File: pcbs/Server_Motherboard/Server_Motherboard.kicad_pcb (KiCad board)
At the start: 2 copper layers, 53 x 70.4 mm, 96 parts, among them IC1 BTM9011EPXUMA1, IC10 BTM9011EPXUMA1, IC11 BTM9011EPXUMA1, IC12 BTM9011EPXUMA1, IC13 BTM9011EPXUMA1, IC14 BTM9011EPXUMA1, IC15 BTM9011EPXUMA1, IC16 BTM9011EPXUMA1, IC17 BTM9011EPXUMA1, IC18 BTM9011EPXUMA1, IC19 BTM9011EPXUMA1, IC2 BTM9011EPXUMA1, IC20 BTM9011EPXUMA1, IC3 BTM9011EPXUMA1, IC4 BTM9011EPXUMA1, IC5 BTM9011EPXUMA1, IC6 BTM9011EPXUMA1, IC7 BTM9011EPXUMA1, IC8 BTM9011EPXUMA1, IC9 BTM9011EPXUMA1, J1 GSB1C41110SSHR, U1 ESP32-C3-MINI-1-H4X

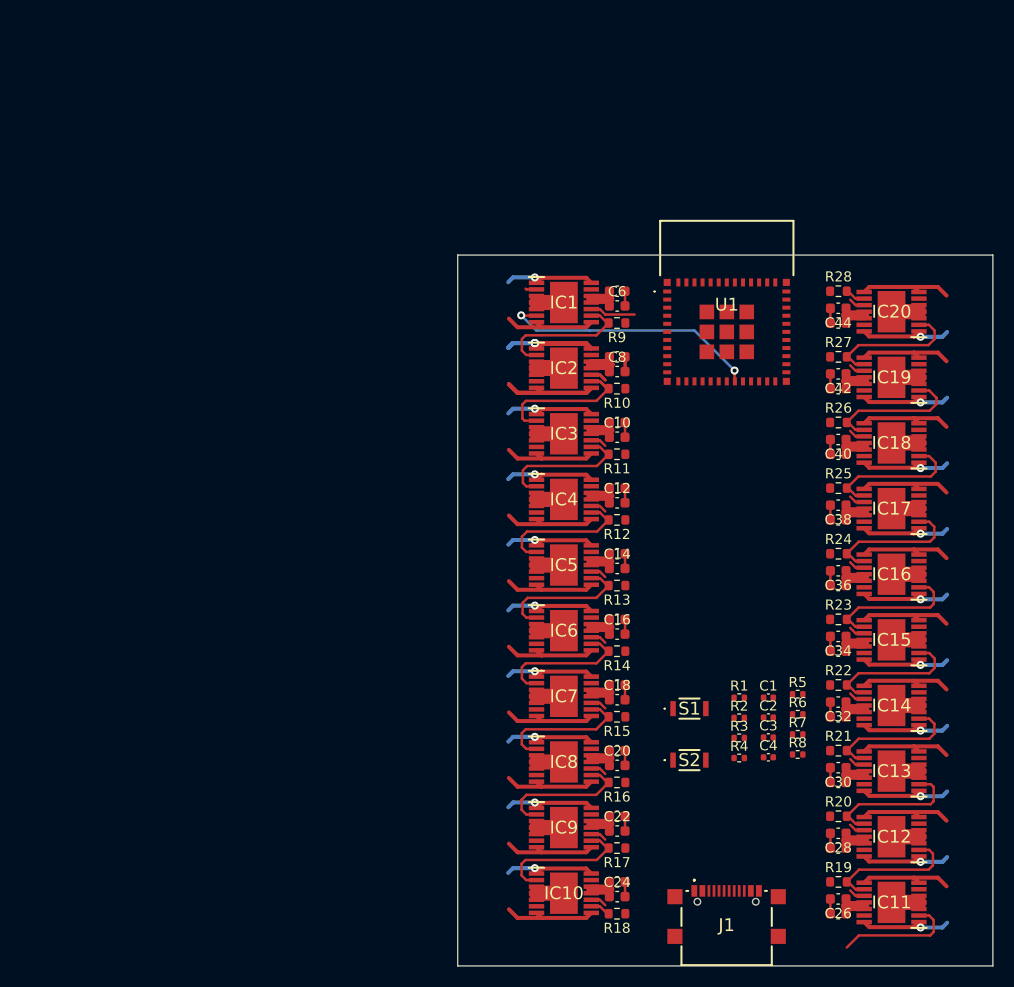
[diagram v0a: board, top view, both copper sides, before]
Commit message: mostly finished server pcb, added pogo charge pins to bots, started charge case pcb
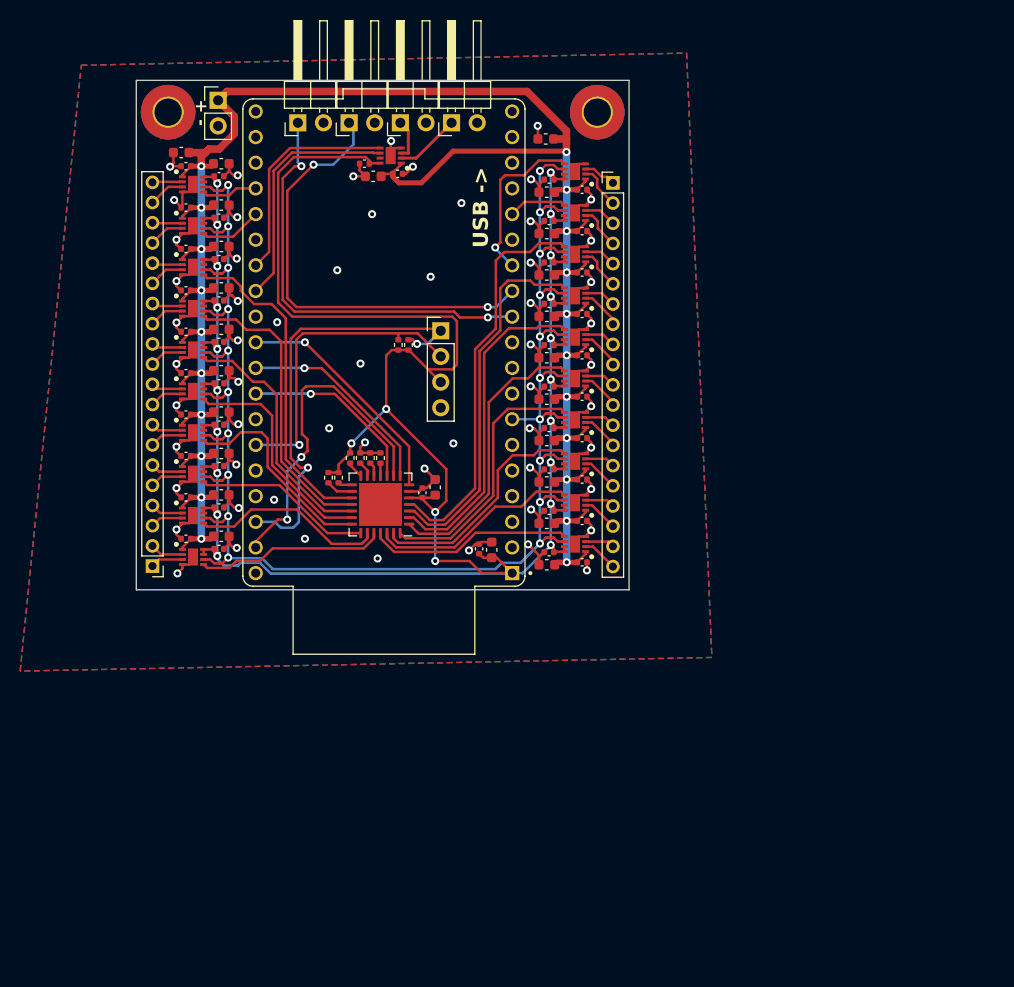
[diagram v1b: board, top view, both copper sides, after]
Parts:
- removed IC10, IC11, IC12, IC13, IC14, IC15, IC16, IC17, IC18, IC19, IC2, IC20, IC3, IC4, IC5, IC6, IC7, IC8, IC9: BTM9011EPXUMA1, SamacSys_Parts:SOP65P600X115-15N
- removed R10, R11, R12, R13, R14, R15, R16, R17, R18, R19, R20, R21, R22, R23, R24, R25, R26, R27, R28, R9: 1k, Resistor_SMD:R_0603_1608Metric
- removed S1, S2: EVP-AWBD4A, SamacSys_Parts:EVPAWBD4A
- added C45: 0.1uF, Capacitor_SMD:C_0402_1005Metric, F.Cu at (57.1, 50.9)
- added C46: 0.1uF, Capacitor_SMD:C_0402_1005Metric, F.Cu at (57.1, 55.0)
- added C47: 0.1uF, Capacitor_SMD:C_0402_1005Metric, F.Cu at (57.1, 59.1)
- added C48: 0.1uF, Capacitor_SMD:C_0402_1005Metric, F.Cu at (57.1, 63.2)
- added C49: 0.1uF, Capacitor_SMD:C_0402_1005Metric, F.Cu at (57.1, 67.3)
- added C50: 0.1uF, Capacitor_SMD:C_0402_1005Metric, F.Cu at (57.1, 71.4)
- added C51: 0.1uF, Capacitor_SMD:C_0402_1005Metric, F.Cu at (57.1, 75.5)
- added C52: 0.1uF, Capacitor_SMD:C_0402_1005Metric, F.Cu at (57.1, 79.6)
- added C53: 0.1uF, Capacitor_SMD:C_0402_1005Metric, F.Cu at (89.8, 79.9)
- added C54: 0.1uF, Capacitor_SMD:C_0402_1005Metric, F.Cu at (89.8, 75.8)
- added C55: 0.1uF, Capacitor_SMD:C_0402_1005Metric, F.Cu at (89.8, 71.7)
- added C56: 0.1uF, Capacitor_SMD:C_0402_1005Metric, F.Cu at (89.8, 67.6)
- added C57: 0.1uF, Capacitor_SMD:C_0402_1005Metric, F.Cu at (89.8, 63.5)
- added C58: 0.1uF, Capacitor_SMD:C_0402_1005Metric, F.Cu at (89.8, 59.4)
- added C59: 0.1uF, Capacitor_SMD:C_0402_1005Metric, F.Cu at (89.8, 55.3)
- added C60: 0.1uF, Capacitor_SMD:C_0402_1005Metric, F.Cu at (89.8, 51.2)
- added C61: 0.1uF, Capacitor_SMD:C_0402_1005Metric, F.Cu at (89.8, 47.1)
- added C62: 0.1uF, Capacitor_SMD:C_0402_1005Metric, F.Cu at (89.8, 43.0)
- added C63: 0.1uF, Capacitor_SMD:C_0402_1005Metric, F.Cu at (77.2, 74.0)
- added C64: 10uF, Capacitor_SMD:C_0603_1608Metric, F.Cu at (78.5, 73.5)
- added C65: 10uF, Capacitor_SMD:C_0603_1608Metric, F.Cu at (84.1, 79.7)
- added C66: 10uF, Capacitor_SMD:C_0603_1608Metric, F.Cu at (89.5, 39.0)
- added C67: 0.1uF, Capacitor_SMD:C_0402_1005Metric, F.Cu at (71.5, 41.4)
- added C68: 10uF, Capacitor_SMD:C_0603_1608Metric, F.Cu at (72.4, 42.6)
- added C69: 0.1uF, Capacitor_SMD:C_0402_1005Metric, F.Cu at (74.8, 42.4)
- added H1: MountingHole_Pad, MountingHole:MountingHole_2.7mm_M2.5_Pad_TopBottom, F.Cu at (52.0, 36.3)
- added H2: MountingHole_Pad, MountingHole:MountingHole_2.7mm_M2.5_Pad_TopBottom, F.Cu at (94.5, 36.3)
- added IC21: DRV8210DSGR, minibot:SON50P200X200X80-9N, F.Cu at (54.5, 43.5)
- added IC22: DRV8210DSGR, minibot:SON50P200X200X80-9N, F.Cu at (54.5, 47.5)
- added IC23: DRV8210DSGR, minibot:SON50P200X200X80-9N, F.Cu at (54.5, 51.6)
- added IC24: DRV8210DSGR, minibot:SON50P200X200X80-9N, F.Cu at (54.5, 55.8)
- added IC25: DRV8210DSGR, minibot:SON50P200X200X80-9N, F.Cu at (54.5, 59.9)
- added IC26: DRV8210DSGR, minibot:SON50P200X200X80-9N, F.Cu at (54.5, 64.0)
- added IC27: DRV8210DSGR, minibot:SON50P200X200X80-9N, F.Cu at (54.5, 68.0)
- added IC28: DRV8210DSGR, minibot:SON50P200X200X80-9N, F.Cu at (54.5, 72.2)
- added IC29: DRV8210DSGR, minibot:SON50P200X200X80-9N, F.Cu at (54.5, 76.2)
- added IC30: DRV8210DSGR, minibot:SON50P200X200X80-9N, F.Cu at (54.5, 80.3)
- added IC31: DRV8210DSGR, minibot:SON50P200X200X80-9N, F.Cu at (92.4, 79.1)
- added IC32: DRV8210DSGR, minibot:SON50P200X200X80-9N, F.Cu at (92.4, 75.0)
- added IC33: DRV8210DSGR, minibot:SON50P200X200X80-9N, F.Cu at (92.4, 70.9)
- added IC34: DRV8210DSGR, minibot:SON50P200X200X80-9N, F.Cu at (92.4, 66.8)
- added IC35: DRV8210DSGR, minibot:SON50P200X200X80-9N, F.Cu at (92.4, 62.7)
- added IC36: DRV8210DSGR, minibot:SON50P200X200X80-9N, F.Cu at (92.4, 58.6)
- added IC37: DRV8210DSGR, minibot:SON50P200X200X80-9N, F.Cu at (92.4, 54.5)
- added IC38: DRV8210DSGR, minibot:SON50P200X200X80-9N, F.Cu at (92.4, 50.4)
- added IC39: DRV8210DSGR, minibot:SON50P200X200X80-9N, F.Cu at (92.4, 46.3)
- added IC40: DRV8210DSGR, minibot:SON50P200X200X80-9N, F.Cu at (92.4, 42.2)
- added J2: Conn_01x20, Connector_PinHeader_2.00mm:PinHeader_1x20_P2.00mm_Vertical, F.Cu at (96.1, 43.3)
- added J3: Conn_01x02, Connector_PinHeader_2.54mm:PinHeader_1x02_P2.54mm_Vertical, F.Cu at (57.0, 35.1)
- added J4: Conn_01x04, Connector_PinHeader_2.54mm:PinHeader_1x04_P2.54mm_Vertical, F.Cu at (79.0, 58.0)
- added J5: Conn_01x02, Connector_PinHeader_2.54mm:PinHeader_1x02_P2.54mm_Horizontal, F.Cu at (75.0, 37.4)
- added J6: Conn_01x02, Connector_PinHeader_2.54mm:PinHeader_1x02_P2.54mm_Horizontal, F.Cu at (80.1, 37.4)
- added J7: Conn_01x02, Connector_PinHeader_2.54mm:PinHeader_1x02_P2.54mm_Horizontal, F.Cu at (64.9, 37.4)
- added J8: Conn_01x02, Connector_PinHeader_2.54mm:PinHeader_1x02_P2.54mm_Horizontal, F.Cu at (70.0, 37.4)
- added U2: MCP23S17_ML, Package_DFN_QFN:QFN-28-1EP_6x6mm_P0.65mm_EP4.25x4.25mm, F.Cu at (73.1, 75.2)
- C1: value 4.7uF -> 10uF; footprint Capacitor_SMD:C_0402_1005Metric -> Capacitor_SMD:C_0603_1608Metric
- C10, C12, C14, C16, C18, C20, C22, C24, C26, C28, C30, C32, C34, C36, C38, C40, C42, C44, C6, C8: footprint Capacitor_SMD:C_0603_1608Metric -> Capacitor_SMD:C_0402_1005Metric
- C2: value 1uF -> 0.1uF
- C3: value 0.1uF -> 10uF; footprint Capacitor_SMD:C_0402_1005Metric -> Capacitor_SMD:C_0603_1608Metric
- C43: value 10uF -> 0.1uF; footprint Capacitor_SMD:C_0603_1608Metric -> Capacitor_SMD:C_0402_1005Metric
- IC1: value BTM9011EPXUMA1 -> DRV8210DSGR; footprint SamacSys_Parts:SOP65P600X115-15N -> minibot:SON50P200X200X80-9N
- J1: value GSB1C41110SSHR -> Conn_01x20; footprint SamacSys_Parts:GSB1C41110SSHR -> Connector_PinHeader_2.00mm:PinHeader_1x20_P2.00mm_Vertical
- R4, R5, R7, R8: value 5.1k -> 10k
- U1: value ESP32-C3-MINI-1-H4X -> ESP32-DEVKITC-32E; footprint SamacSys_Parts:ESP32C3MINI1H4X -> minibot:MODULE_ESP32-DEVKITC-32E
- moved C4 82.2 mm to (53.8, 41.6), turned to 180 degrees
- moved C1 79.3 mm to (53.4, 40.3)
- moved C3 78.5 mm to (57.3, 41.4)
- moved J1 67.1 mm to (50.5, 81.2), turned to 180 degrees
- moved C43 63.0 mm to (57.1, 42.7), turned to 0 degrees
- moved C44 62.0 mm to (57.1, 46.8), turned to 0 degrees
- moved R8 53.1 mm to (68.9, 72.5), turned to -90 degrees
- moved R7 53.0 mm to (67.9, 72.5), turned to -90 degrees
- moved C22 51.6 mm to (53.8, 78.5), turned to 180 degrees
- moved R6 51.1 mm to (70.1, 70.5), turned to -90 degrees
- moved C20 50.3 mm to (53.8, 74.5), turned to 180 degrees
- moved R2 50.0 mm to (74.8, 59.4), turned to 90 degrees
- moved R5 49.2 mm to (71.1, 70.5), turned to 90 degrees
- moved C18 49.1 mm to (53.8, 70.3), turned to 180 degrees
- moved C25 48.2 mm to (89.6, 77.0)
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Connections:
- C1 pad 2: +3V3 -> VDC
- C2 pad 1: /RST -> +3V3
- C3 pad 1: +3V3 -> VDC
- C4 pad 1: /GPIO9 -> VDC
- C43 pad 1: VDC -> +3V3
- C44 pad 1: VDC -> +3V3
- IC1 pad 1: /COIL0_A -> VDC
- IC1 pad 2: /SDI -> /SOL_1
- IC1 pad 3: GND -> /SOL_0
- IC1 pad 5: GND -> /SOL_EN_1
- IC1 pad 6: /SCLK -> /SOL_EN_0
- IC1 pad 7: /COIL0_B -> unconnected-(IC1-MODE-Pad7)
- IC1 pad 8: /COIL0_B -> +3V3
- IC1 pad 9: /SDIO_1 -> GND
- R1 pad 2: /GPIO8 -> /SCL
- R2 pad 2: /RST -> /SDA
- R3 pad 1: +3V3 -> /A0
- R3 pad 2: /GPIO2 -> GND
- R4 pad 1: +3V3 -> /A1
- R4 pad 2: /SCL -> GND
- R5 pad 1: +3V3 -> /A2
- R5 pad 2: /SDA -> GND
- R6 pad 2: /GPIO9 -> /RESET
- R7 pad 1: /CC1 -> +3V3
- R7 pad 2: GND -> /INTA
- R8 pad 1: /CC2 -> +3V3
- R8 pad 2: GND -> /INTB
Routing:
- net +3V3: track 0.00 -> 263.3 mm, vias 0 -> 24
- net /COIL_DIR: track 0.00 -> 165.5 mm, vias 0 -> 20
- net VDC: track 85.9 -> 250.9 mm, vias 0 -> 21
- net /SW2: track 0.00 -> 44.5 mm, vias 0 -> 2
- net /SCL: track 0.00 -> 43.7 mm, vias 0 -> 2
- net /SW1: track 0.00 -> 42.3 mm, vias 0 -> 2
- net /C_EN_17: track 0.00 -> 39.5 mm
- net /CS: track 38.3 -> 0.00 mm
- net /C_EN_16: track 0.00 -> 36.8 mm
- net GND: track 120.4 -> 156.3 mm, vias 0 -> 59
- net /MOSI: track 0.00 -> 33.1 mm, vias 0 -> 2
- net /C_EN_15: track 0.00 -> 32.4 mm
- net /C_EN_2: track 0.00 -> 32.3 mm
- net /SDA: track 0.00 -> 31.0 mm, vias 0 -> 1
- net /C_EN_3: track 0.00 -> 29.4 mm
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- added copper zone on B.Cu, net GND
- added copper zone on F.Cu, net GND
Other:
- board size 53 x 70.4 mm -> 48.8 x 50.4 mm
- board text added: "+ -"
- board text added: "C0"
- board text added: "C1"
- board text added: "C10"
- board text added: "C11"
- board text added: "C12"
- board text added: "C13"
- board text added: "C14"
- board text added: "C15"
- board text added: "C16"
- board text added: "C17"
- board text added: "C18"
- board text added: "C19"
- board text added: "C2"
- board text added: "C3"
- board text added: "C4"
- board text added: "C5"
- board text added: "C6"
- board text added: "C7"
- board text added: "C8"
- board text added: "C9"
- board text added: "SCL SDA 3V3 GND"
- board text added: "SL1 SL0 SW1 SW0"
- board text added: "USB ->"
